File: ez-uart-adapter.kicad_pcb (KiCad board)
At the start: 2 copper layers, 45 x 15 mm, 23 parts, among them J1 USB_C_Receptacle_USB2.0_16P, J2 Conn_01x04_Pin, Q1 2N7002, Q2 2N7002, Q3 AO3401A, SW1 MK-11C04-G013, U1 USBLC6-2SC6, U2 AP2112K-3.3, U3 CH340C

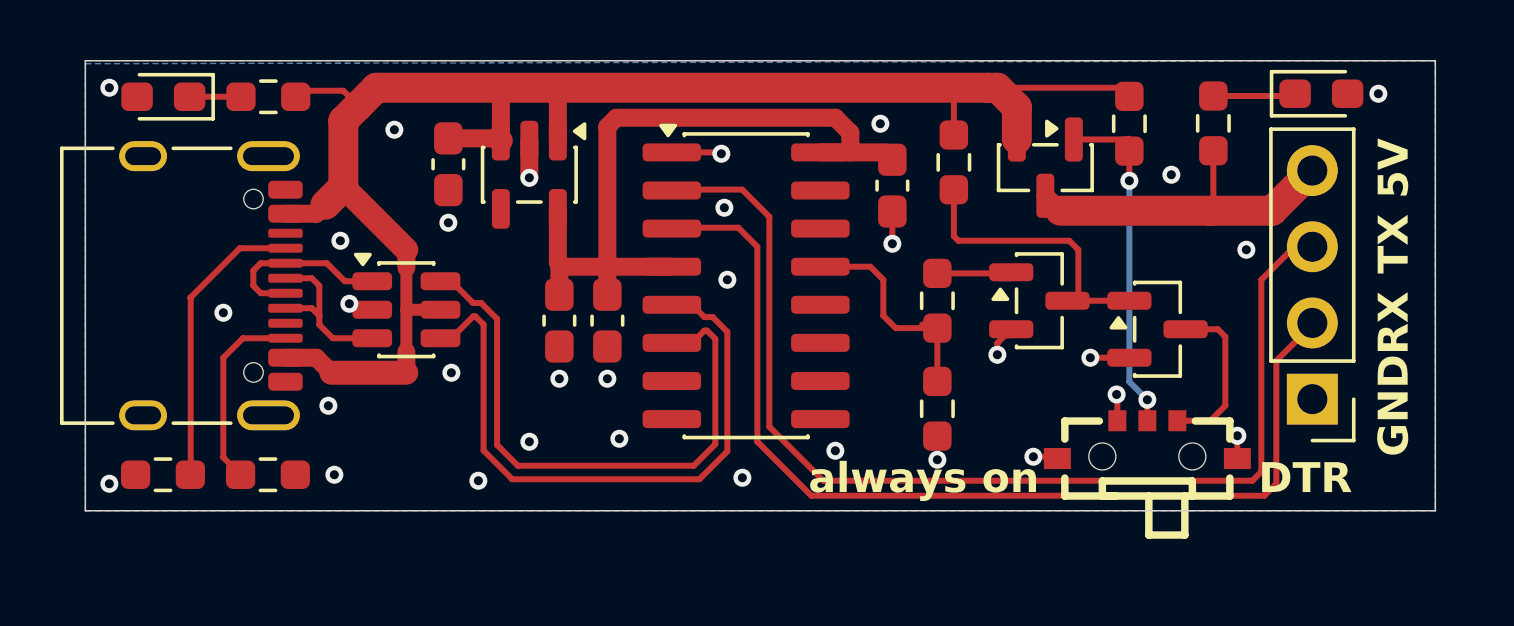
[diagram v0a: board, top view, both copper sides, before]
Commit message: Tweak PCB
Most notably remove the top ground pour. Experts say that especially on
two-layer boards they cause more harm than good.
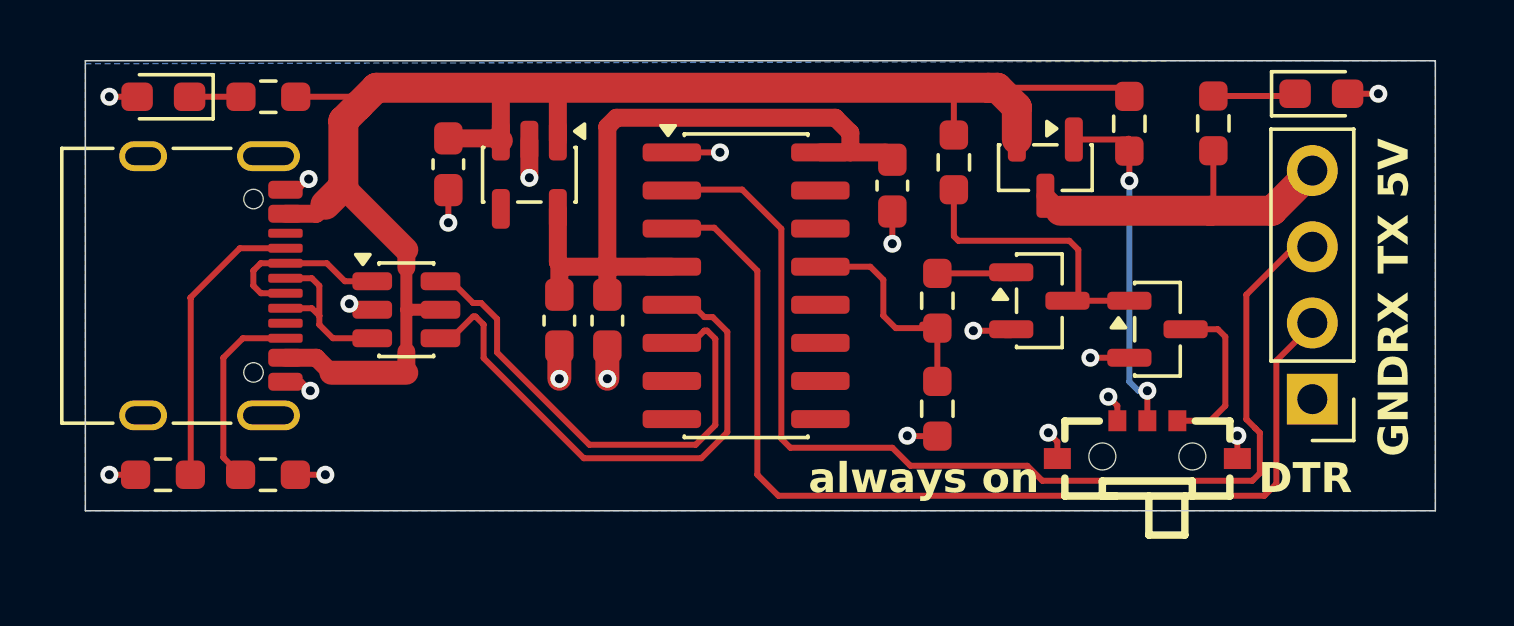
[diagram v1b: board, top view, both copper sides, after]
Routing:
- net GND: track 9.28 -> 19.3 mm, vias 32 -> 19
- net /UD+: track 21.2 -> 18.4 mm
- net /UD-: track 20.3 -> 17.6 mm
- removed copper zone on F.Cu, net GND
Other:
- board text added: "EZ USB-UART ADAPTER 1.1"
- board text removed: "EZ USB-UART ADAPTER 1.0"

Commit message: Add ESD protection to UART
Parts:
- added R10: 470R, Resistor_SMD:R_0603_1608Metric_Pad0.98x0.95mm_HandSolder, F.Cu at (164.4, 108.9)
- added R9: 470R, Resistor_SMD:R_0603_1608Metric_Pad0.98x0.95mm_HandSolder, F.Cu at (164.4, 104.7)
- moved SW1 2.20 mm to (159.2, 110.1)
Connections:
- J2 pad 2: RX -> Net-(J2-Pin_2)
- J2 pad 3: TX -> Net-(J2-Pin_3)
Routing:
- net RX: track 34.0 -> 28.6 mm
- net TX: track 36.6 -> 32.0 mm
- net Net-(J2-Pin_2): track 0.00 -> 3.22 mm
- net Net-(J2-Pin_3): track 0.00 -> 2.81 mm
- net Net-(Q3-G): track 11.5 -> 12.4 mm

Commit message: fixup! Add ESD protection to UART
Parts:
- added D3: PSM712, Package_TO_SOT_SMD:SOT-23, F.Cu at (170.0, 112.7)
- moved Q1 1.80 mm to (156.0, 105.5)
- moved Q2 1.80 mm to (159.9, 106.5)
- moved R9 1.56 mm to (163.0, 104.0), turned to 180 degrees
- moved SW1 1.50 mm to (157.7, 110.1)
- moved R7 1.41 mm to (153.0, 108.9)
- moved R6 1.40 mm to (153.0, 105.5)
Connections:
- D1 pad 1: Net-(D1-K) -> GND
- D1 pad 2: GND -> Net-(D1-A)
- D2 pad 1: Net-(D2-K) -> GND
- D2 pad 2: GND -> Net-(D2-A)
- R1 pad 2: Net-(D1-K) -> Net-(D1-A)
- R8 pad 2: Net-(D2-K) -> Net-(D2-A)
- R9 pad 1: TX -> Net-(J2-Pin_3)
- R9 pad 2: Net-(J2-Pin_3) -> TX
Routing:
- net TX: track 32.0 -> 11.7 mm
- net Net-(J2-Pin_3): track 2.81 -> 14.2 mm
- net Net-(U3-~{DTR}): track 7.90 -> 0.01 mm
- net Net-(Q2-D): track 5.69 -> 0.00 mm
- net RX: track 28.6 -> 26.0 mm
- net Net-(D2-K): track 2.56 -> 0.00 mm
- net Net-(D1-K): track 2.00 -> 0.00 mm
- net Net-(Q1-G): track 3.12 -> 4.52 mm
- net Net-(D2-A): track 0.00 -> 1.03 mm
- net Net-(D1-A): track 0.00 -> 0.92 mm
- net GND: track 19.3 -> 20.0 mm, vias 19 -> 17
